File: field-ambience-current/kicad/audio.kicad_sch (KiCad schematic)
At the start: 29 parts, among them J6 Speaker L (PUI AS04008PS, 4R 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, J7 Speaker R (PUI AS04008PS, 4R 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, J8 3.5mm TRS Line/Headphone Out 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, U3 PCM5102A I²S DAC (TSSOP-20), U4 PAM8403H Class-D Stereo Amp (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

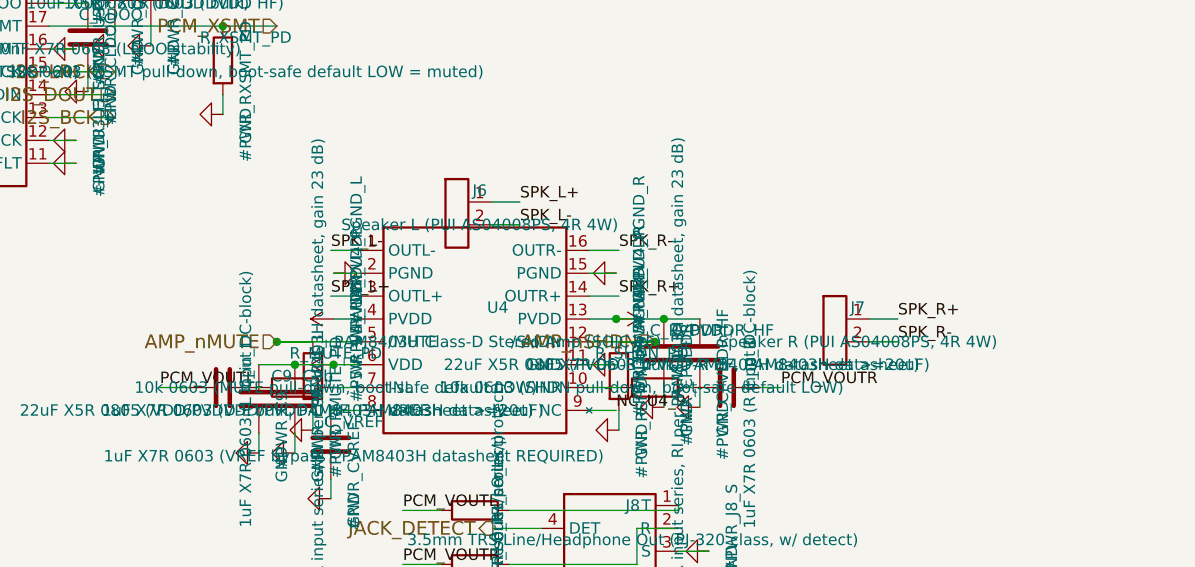
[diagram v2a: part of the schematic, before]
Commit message: pcb(r18.19): Audit-Fixes — USB-C 16-Pin-Revert, Audio-Jack-FP, Speaker-Sync, Regen
Senior-Engineer-Audit deckte vier Defekte auf:

🔴 CRITICAL — USB-C-Stecker-Revert auf 16-Pin M-12
LCSC C283540 (TYPE-C-31-M-17) ist 6-Pin POWER-ONLY (LCSC-Produktseite "6P"):
keine D+/D-, kein CC1/CC2. USB-DFU-Flashen über PA11/PA12 wäre physikalisch
unmöglich gewesen — SW_BOOT-Story aus ADR-0009 wäre kaputt, alle
USB_DM/USB_DP/CC-Pads im Schaltplan floateten. Revert auf C165948
(TYPE-C-31-M-12, 16-Pin volle USB-C-Belegung, 168k+ Stock). Insertion-
Cycle-Trade-Off 10k → ~5k bewusst akzeptiert. Lehre: Pin-Count immer aus
Produktseite verifizieren, nicht aus "drop-in laut Bauform" ableiten.

🟠 HIGH — Audio-Jack-Footprint inkompatibel zum verbauten Teil
J8/J9 hatten Connector_Audio:Jack_3.5mm_CUI_SJ-3523-SMT_Horizontal
zugewiesen. Verbaut wird C431535 (SHOU HAN PJ-320D) mit anderem Pad-Layout
(4 SMD-Pads bei 2.8mm-Pitch + 2 NPTH-Posts). Assembly wäre gescheitert.
EasyEDA-CAD-verifizierter Footprint in Project-Lib vendored als
field_ambience:Jack_3.5mm_PJ-320D_SMT (gleiche Methodik wie SW_TS1088).

🟠 HIGH — Speaker-Wert im Audio-Sheet seit r18.18 stale
J6/J7 hatten value="Speaker L/R (PUI AS04008PS, 4R 4W)" + MPN PUI AS04008.
Drei Fehler: 4Ω (seit r14 als 8Ω korrigiert; Power-Budget rechnet 8Ω),
PUI statt CMS-402811-28SP (r18.18 Primärwahl), Papier-Variante.
Aktualisiert auf "Same Sky CMS-402811-28SP Cloth-Cone 8R 2W".

🟠 CRITICAL (Prozess) — Generator seit r18.14b nicht regeneriert
Alle Entscheidungen r18.15–r18.18 lebten nur in Docs. Schematic (einzige
Netlist-Quelle) hing auf r18.14b. Mit r18.19 erstmals wieder regeneriert.

Verifizierung:
- 8/8 .kicad_sch paren-balanced
- USB-C: 4× C165948/M-12 in power_tree, 0 ungewollte M-17-Leftovers
- Jack-FP: 1× field_ambience:Jack_3.5mm_PJ-320D_SMT in audio, 0 CUI-Leftovers
- Speaker: 6× CMS-402811-28SP, 0 "PUI 4R" Leftovers
- Firmware 13/13 Suiten PASS

Files: generate_kicad_project.py (3 Edits + speaker MPN props),
field_ambience.pretty/Jack_3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
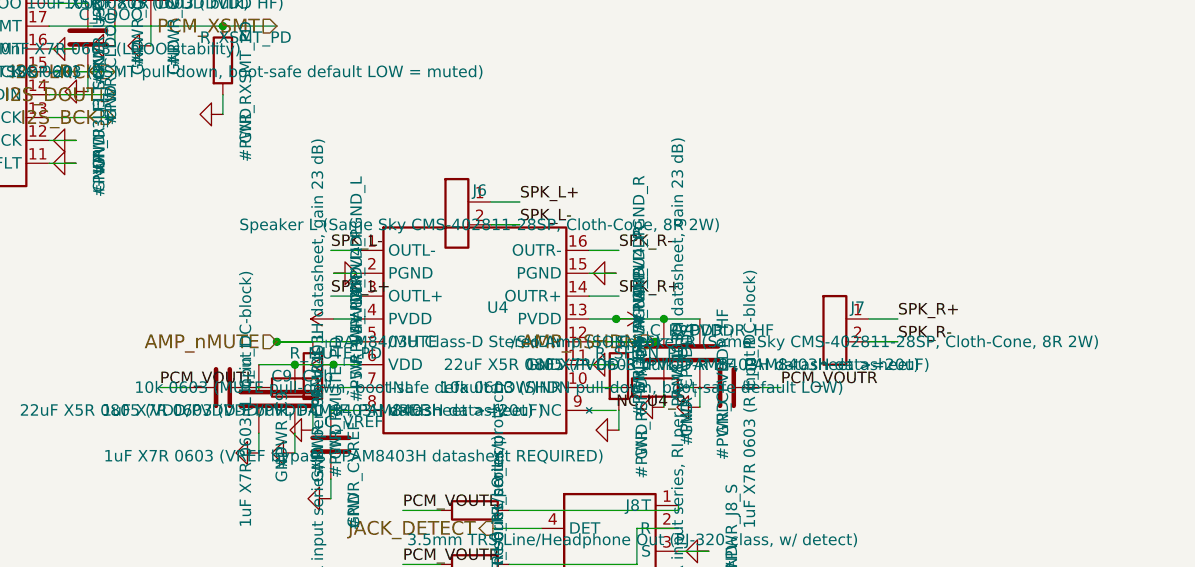
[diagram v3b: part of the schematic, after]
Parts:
- J6: value Speaker L (PUI AS04008PS, 4R 4W) -> Speaker L (Same Sky CMS-402811-28SP, Cloth-Cone, 8R 2W); LCSC TBD -> TBD (kein LCSC-Stock fuer 40mm-Treiber; DigiKey 102-CMS-402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; MPN AS04008PS-4W-WR-R -> Same Sky CMS-402811-28SP (Cloth-Cone primaer; PUI AS04008PS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; Notes (none) -> Treiber haengt vom Top-Panel (Top-Firing, ADR-0007/ADR-0011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
- J7: value Speaker R (PUI AS04008PS, 4R 4W) -> Speaker R (Same Sky CMS-402811-28SP, Cloth-Cone, 8R 2W); LCSC TBD -> TBD (kein LCSC-Stock fuer 40mm-Treiber; DigiKey 102-CMS-402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; MPN AS04008PS-4W-WR-R -> Same Sky CMS-402811-28SP (Cloth-Cone primaer; PUI AS04008PS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; Notes (none) -> Treiber haengt vom Top-Panel (Top-Firing, ADR-0007/ADR-0011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
- J8: footprint Connector_Audio:Jack_3.5mm_CUI_SJ-3523-SMT_Horizontal -> field_ambience:Jack_3.5mm_PJ-320D_SMT
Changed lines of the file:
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@@
       (property "Reference" "J6" (at 160.54 114.46 0)
         (effects (font (size 1.27 1.27))))
-      (property "Value" "Speaker L (PUI AS04008PS, 4R 4W)" (at 160.54 118.27 0)
+      (property "Value" "Speaker L (Same Sky CMS-402811-28SP, Cloth-Cone, 8R 2W)" (at 160.54 118.27 0)
         (effects (font (size 1.27 1.27))))
       (property "Footprint" "Connector_PinHeader_2.54mm:PinHeader_1x02_P2.54mm_Vertical" (at 158 117 0)
@@
       (property "Datasheet" "~" (at 158 117 0)
         (effects (font (size 1.27 1.27)) hide))
-      (property "MPN" "AS04008PS-4W-WR-R" (at 160.54 120.81 0)
+      (property "MPN" "Same Sky CMS-402811-28SP (Cloth-Cone primaer; PUI AS04008PS-4W-WR-R sekundaer)" (at 160.54 120.81 0)
         (effects (font (size 1.27 1.27)) hide))
-      (property "LCSC" "TBD" (at 160.54 122.08 0)
+      (property "LCSC" "TBD (kein LCSC-Stock fuer 40mm-Treiber; DigiKey 102-CMS-402811-28SP-ND)" (at 160.54 122.08 0)
+        (effects (font (size 1.27 1.27)) hide))
+      (property "Notes" "Treiber haengt vom Top-Panel (Top-Firing, ADR-0007/ADR-0011), kein PCB-Mount. J6/J7 sind nur 2-Pin-Loetpads; Draht zum Treiber-Eyelet manuell. r18.18: Cloth-Cone-Wechsel." (at 160.54 123.35 0)
         (effects (font (size 1.27 1.27)) hide))
     (instances
@@
       (property "Reference" "J7" (at 202.54 127.46 0)
         (effects (font (size 1.27 1.27))))
-      (property "Value" "Speaker R (PUI AS04008PS, 4R 4W)" (at 202.54 131.27 0)
+      (property "Value" "Speaker R (Same Sky CMS-402811-28SP, Cloth-Cone, 8R 2W)" (at 202.54 131.27 0)
         (effects (font (size 1.27 1.27))))
       (property "Footprint" "Connector_PinHeader_2.54mm:PinHeader_1x02_P2.54mm_Vertical" (at 200 130 0)
@@
       (property "Datasheet" "~" (at 200 130 0)
         (effects (font (size 1.27 1.27)) hide))
-      (property "MPN" "AS04008PS-4W-WR-R" (at 202.54 133.81 0)
+      (property "MPN" "Same Sky CMS-402811-28SP (Cloth-Cone primaer; PUI AS04008PS-4W-WR-R sekundaer)" (at 202.54 133.81 0)
         (effects (font (size 1.27 1.27)) hide))
-      (property "LCSC" "TBD" (at 202.54 135.08 0)
+      (property "LCSC" "TBD (kein LCSC-Stock fuer 40mm-Treiber; DigiKey 102-CMS-402811-28SP-ND)" (at 202.54 135.08 0)
+        (effects (font (size 1.27 1.27)) hide))
+      (property "Notes" "Treiber haengt vom Top-Panel (Top-Firing, ADR-0007/ADR-0011), kein PCB-Mount. J6/J7 sind nur 2-Pin-Loetpads; Draht zum Treiber-Eyelet manuell. r18.18: Cloth-Cone-Wechsel." (at 202.54 136.35 0)
         (effects (font (size 1.27 1.27)) hide))
     (instances
@@
       (property "Value" "3.5mm TRS Line/Headphone Out (PJ-320 class, w/ detect)" (at 177.54 153.27 0)
         (effects (font (size 1.27 1.27))))
-      (property "Footprint" "Connector_Audio:Jack_3.5mm_CUI_SJ-3523-SMT_Horizontal" (at 175.0 152.0 0)
+      (property "Footprint" "field_ambience:Jack_3.5mm_PJ-320D_SMT" (at 175.0 152.0 0)
         (effects (font (size 1.27 1.27)) hide))
       (property "Datasheet" "~" (at 175.0 152.0 0)
